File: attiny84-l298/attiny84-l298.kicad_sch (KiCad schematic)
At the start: 0 parts

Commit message: attiny84-l298 V0.1 Schematic
Signed-off-by: Matthew Nickson <mnickson@sidingsmedia.com>
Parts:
- added C1, C2, C3, C4, C5: 0.1uF, symbol Device:C
- added D1, D2, D3, D4: D, symbol Device:D
- added J1: DIN41612_02x16_AB, symbol Connector:DIN41612_02x16_AB
- added J2, J3, J4, J5: Banana Socket, symbol Connector:Conn_01x01_Female
- added R1, R2, R3, R4, R5, R6, R7, R8, R9: 1K, symbol Device:R
- added R10: 4.7K, symbol Device:R
- added R11: 0.5R, symbol Device:R
- added SW1: SW_DIP_x08, symbol Switch:SW_DIP_x08
- added U1: 74151, symbol 74xx_IEEE:74151
- added U2: ATtiny84A-P, Package_DIP:DIP-14_W7.62mm, symbol MCU_Microchip_ATtiny:ATtiny84A-P
- added U3: L298HN, Package_TO_SOT_THT:TO-220-15_P2.54x2.54mm_StaggerOdd_Lead5.84mm_TabDown, symbol Driver_Motor:L298HN
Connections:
- new net: R5.1, SW1.12, U1.15 (I4)
- new net: R8.1, SW1.9, U1.12 (I7)
- new net: D3.2 (A), D4.1 (K), J5.1 (Pin_1), U3.14 (OUT4), U3.3 (OUT2)
- new net: R6.1, SW1.11, U1.14 (I5)
- new net: R3.1, SW1.14, U1.2 (I2)
- new net: R4.1, SW1.13, U1.1 (I3)
- new net: D1.2 (A), D2.1 (K), J4.1 (Pin_1), U3.13 (OUT3), U3.2 (OUT1)
- new net: C5.1, D1.1 (K), D3.1 (K), J2.1 (Pin_1), U3.4 (Vs)
- new net: R7.1, SW1.10, U1.13 (I6)
- new net: R2.1, SW1.15, U1.3 (I1)
- new net: R1.1, SW1.16, U1.4 (I0)
- new net +12V: J1.a1 (Pin_a1), J1.a2 (Pin_a2)
- new net +1V1: J1.b5 (Pin_b5), J1.b6 (Pin_b6)
- new net +3V3: J1.a5 (Pin_a5), J1.a6 (Pin_a6)
- new net +5V: C1.1, C2.1, C4.1, J1.b1 (Pin_b1), J1.b2 (Pin_b2), R10.1, R9.1, SW1.1, SW1.2, SW1.3, SW1.4, SW1.5, SW1.6, SW1.7, SW1.8, U1.16 (VCC), U2.1 (VCC), U3.9 (Vss)
- new net -12V: J1.a3 (Pin_a3), J1.a4 (Pin_a4)
- new net -5V: J1.b3 (Pin_b3), J1.b4 (Pin_b4)
- new net GND: C1.2, C2.2, C3.2, C4.2, C5.2, D2.2 (A), D4.2 (A), J1.a7 (Pin_a7), J1.a8 (Pin_a8), J1.a9 (Pin_a9), J1.b7 (Pin_b7), J1.b8 (Pin_b8), J1.b9 (Pin_b9), J3.1 (Pin_1), R1.2, R11.2, R2.2, R3.2, R4.2, R5.2, R6.2, R7.2, R8.2, U1.8 (GND), U2.14 (GND), U3.8 (GND)
- new net I2C_SCL: J1.a15 (Pin_a15), U2.9 (PA4)
- new net I2C_SDA: J1.a16 (Pin_a16), U2.7 (PA6)
- new net L298_EN: U2.10 (PA3), U3.11 (EnB), U3.6 (EnA)
- new net L298_IN2: U2.5 (PB2), U2.6 (PA7), U3.10 (IN3), U3.12 (IN4), U3.5 (IN1), U3.7 (IN2)
- new net L298_SENSE: R11.1, U2.8 (PA5), U3.1 (SENSE_A), U3.15 (SENSE_B)
- new net MUX_OUT: U1.5 (Q), U2.13 (AREF/PA0)
- new net MUX_S0: U1.11 (S0), U2.11 (PA2)
- new net MUX_S1: U1.10 (S1), U2.2 (XTAL1/PB0)
- new net MUX_S2: U1.9 (S2), U2.3 (XTAL2/PB1)
- new net SPI_MISO: J1.a12 (Pin_a12)
- new net SPI_MOSI: J1.a11 (Pin_a11)
- new net SPI_SCLK: J1.a10 (Pin_a10)
- new net SPI_~{CS_{1}}: J1.a13 (Pin_a13)
- new net SPI_~{CS_{2}}: J1.a14 (Pin_a14)
- new net SPI_~{CS_{3}: J1.b16 (Pin_b16)
- new net SPI_~{CS_{4}: J1.b15 (Pin_b15)
- new net UD/NC: J1.b11 (Pin_b11), J1.b12 (Pin_b12), J1.b13 (Pin_b13), J1.b14 (Pin_b14)
- new net ~{MUX_INPUT_EN}: R9.2, U1.7 (~{E}), U2.12 (PA1)
- new net ~{RESET}: C3.1, J1.b10 (Pin_b10), R10.2, U2.4 (~{RESET}/PB3)
- no-connect marks 0 -> 1
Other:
- note added: "Backplane connector"
- note added: "Caps need to be close as posible to GND pin of L298"
- note added: "I2C Address selection"
- note added: "Sense resistor must not be wirewound. Should be grounded near GND pin."
- note added: "Train power in"
- note added: "Train power out"

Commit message: Assigned footprints for attiny84-l298
Signed-off-by: Matthew Nickson <mnickson@sidingsmedia.com>
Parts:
- C1, C2, C3, C4, C5: footprint (none) -> Capacitor_THT:C_Disc_D4.7mm_W2.5mm_P5.00mm
- D1, D2, D3, D4: footprint (none) -> Diode_THT:D_5W_P10.16mm_Horizontal
- J1: footprint (none) -> Connector_DIN:DIN41612_B2_2x16_Male_Horizontal_THT
- J2, J3, J4, J5: footprint (none) -> Connector:Banana_Jack_3Pin
- R1, R10, R2, R3, R4, R5, R6, R7, R8, R9: footprint (none) -> Resistor_THT:R_Axial_DIN0207_L6.3mm_D2.5mm_P7.62mm_Horizontal
- R11: footprint (none) -> Resistor_THT:R_Axial_DIN0617_L17.0mm_D6.0mm_P20.32mm_Horizontal
- SW1, U1: footprint (none) -> Package_DIP:DIP-16_W7.62mm

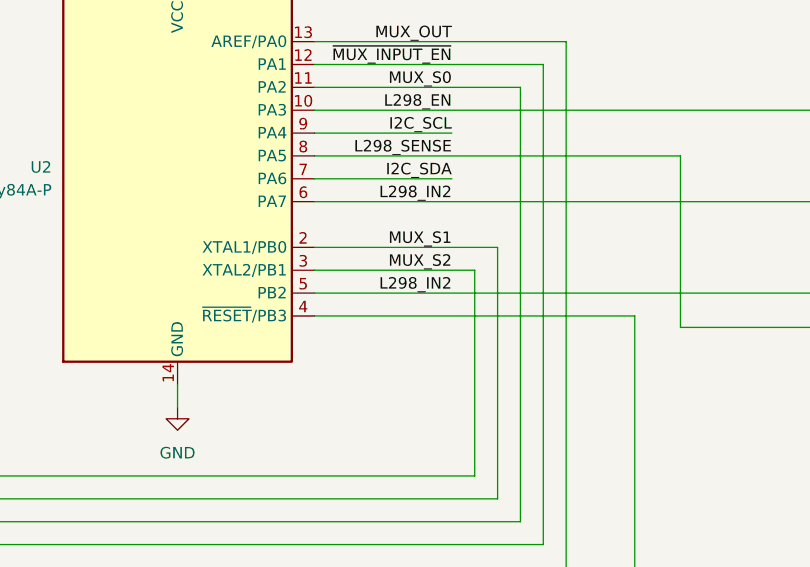
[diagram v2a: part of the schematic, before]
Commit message: Fixed net label name
Signed-off-by: Matthew Nickson <mnickson@sidingsmedia.com>
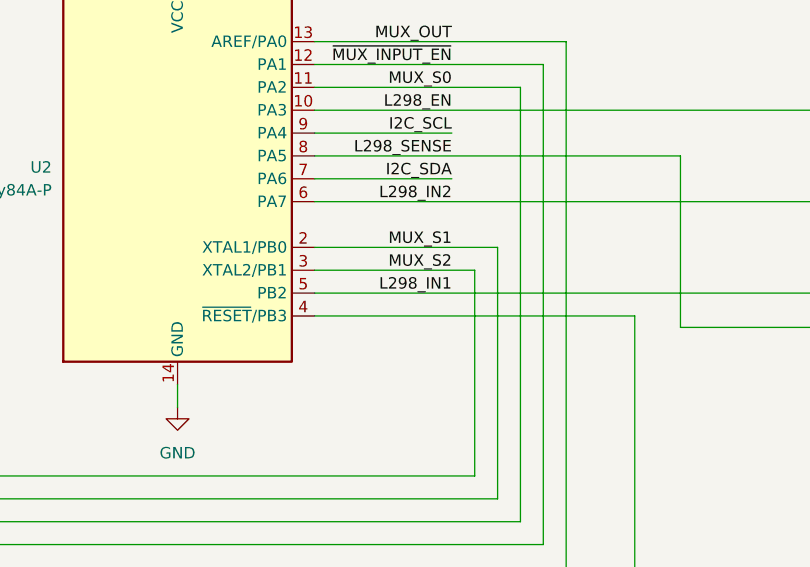
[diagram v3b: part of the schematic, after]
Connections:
- net L298_IN2: no longer U2.5 (PB2), U3.10 (IN3), U3.5 (IN1)
- new net L298_IN1: U2.5 (PB2), U3.10 (IN3), U3.5 (IN1)
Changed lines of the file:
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@@
     (effects (font (size 1.27 1.27)) (justify right bottom))
   )
-  (label "L298_IN2" (at 149.86 83.82 180)
+  (label "L298_IN1" (at 149.86 83.82 180)
     (effects (font (size 1.27 1.27)) (justify right bottom))
   )

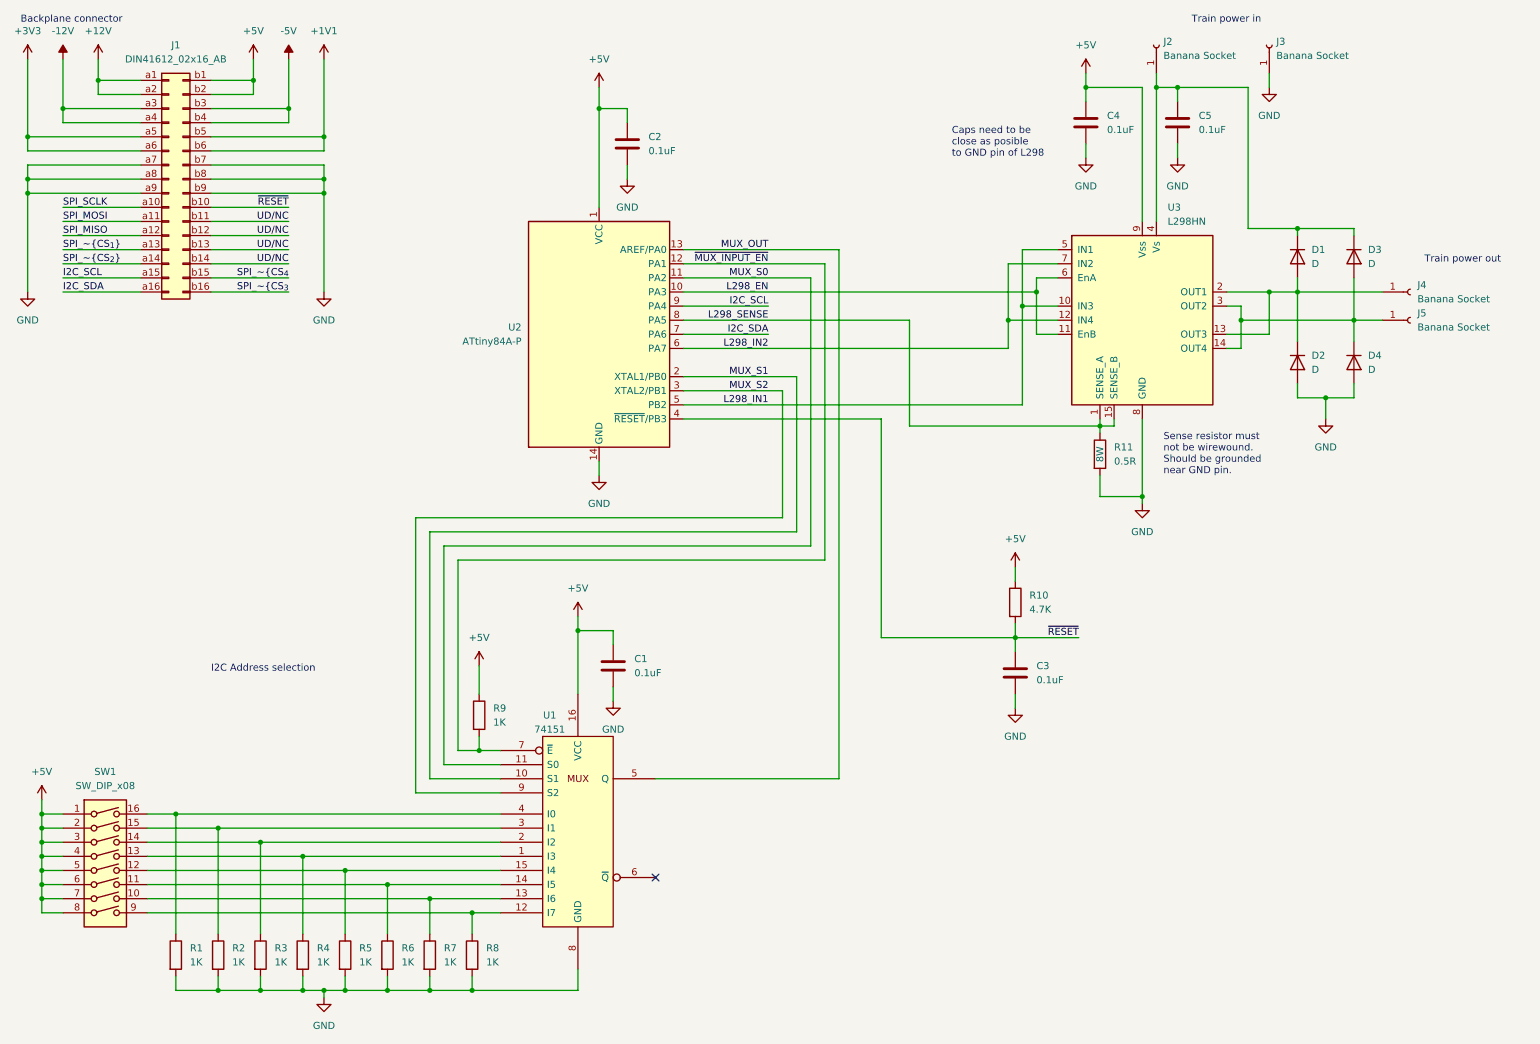
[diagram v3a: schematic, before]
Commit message: Cleaned up schematic and fixed DRC errors
Signed-off-by: Matthew Nickson <mnickson@sidingsmedia.com>
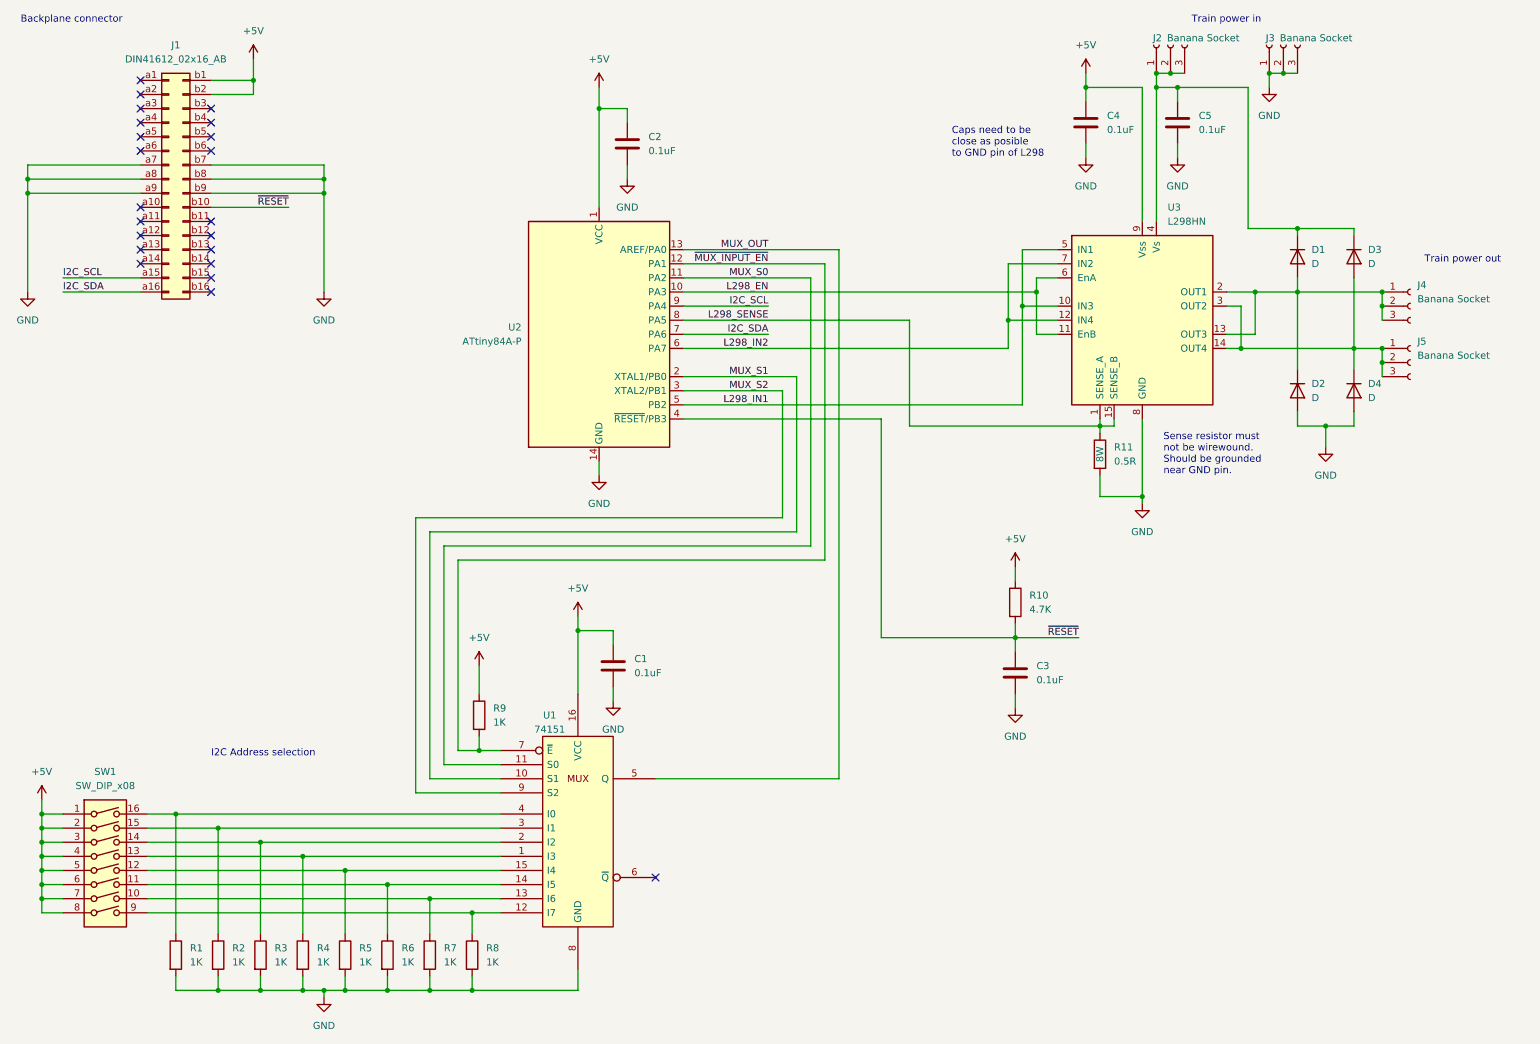
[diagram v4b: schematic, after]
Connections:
- net GND: now also J3.2 (Pin_2), J3.3 (Pin_3)
- net at D3.2 (A), D4.1 (K), J5.1 (Pin_1)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: now also J5.2 (Pin_2), J5.3 (Pin_3)
- net at D1.2 (A), D2.1 (K), J4.1 (Pin_1)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: now also J4.2 (Pin_2), J4.3 (Pin_3)
- net at C5.1, D1.1 (K), D3.1 (K)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: now also J2.2 (Pin_2), J2.3 (Pin_3)
- net +12V: no longer names the net of J1.a1 (Pin_a1)
- net +12V: no longer J1.a2 (Pin_a2)
- net +1V1: no longer names the net of J1.b5 (Pin_b5)
- net +1V1: no longer J1.b6 (Pin_b6)
- net +3V3: no longer names the net of J1.a5 (Pin_a5)
- net +3V3: no longer J1.a6 (Pin_a6)
- net -12V: no longer names the net of J1.a3 (Pin_a3)
- net -12V: no longer J1.a4 (Pin_a4)
- net -5V: no longer names the net of J1.b3 (Pin_b3)
- net -5V: no longer J1.b4 (Pin_b4)
- net SPI_MISO: no longer names the net of J1.a12 (Pin_a12)
- net SPI_MOSI: no longer names the net of J1.a11 (Pin_a11)
- net SPI_SCLK: no longer names the net of J1.a10 (Pin_a10)
- net SPI_~{CS_{1}}: no longer names the net of J1.a13 (Pin_a13)
- net SPI_~{CS_{2}}: no longer names the net of J1.a14 (Pin_a14)
- net SPI_~{CS_{3}: no longer names the net of J1.b16 (Pin_b16)
- net SPI_~{CS_{4}: no longer names the net of J1.b15 (Pin_b15)
- removed net UD/NC: J1.b11 (Pin_b11), J1.b12 (Pin_b12), J1.b13 (Pin_b13), J1.b14 (Pin_b14)
- no-connect marks 1 -> 22
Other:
- moved on the sheet: D2, D4
